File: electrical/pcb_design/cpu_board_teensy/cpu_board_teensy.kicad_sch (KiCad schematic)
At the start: 9 parts, among them J1 Molex_504050-1291, U1 Teensy4.0_TopPinsOnly, U2 RFM69HCW, U3 BNO085_Adafruit_Breakout_I2C, U4 BMP390_Adafruit_Breakout

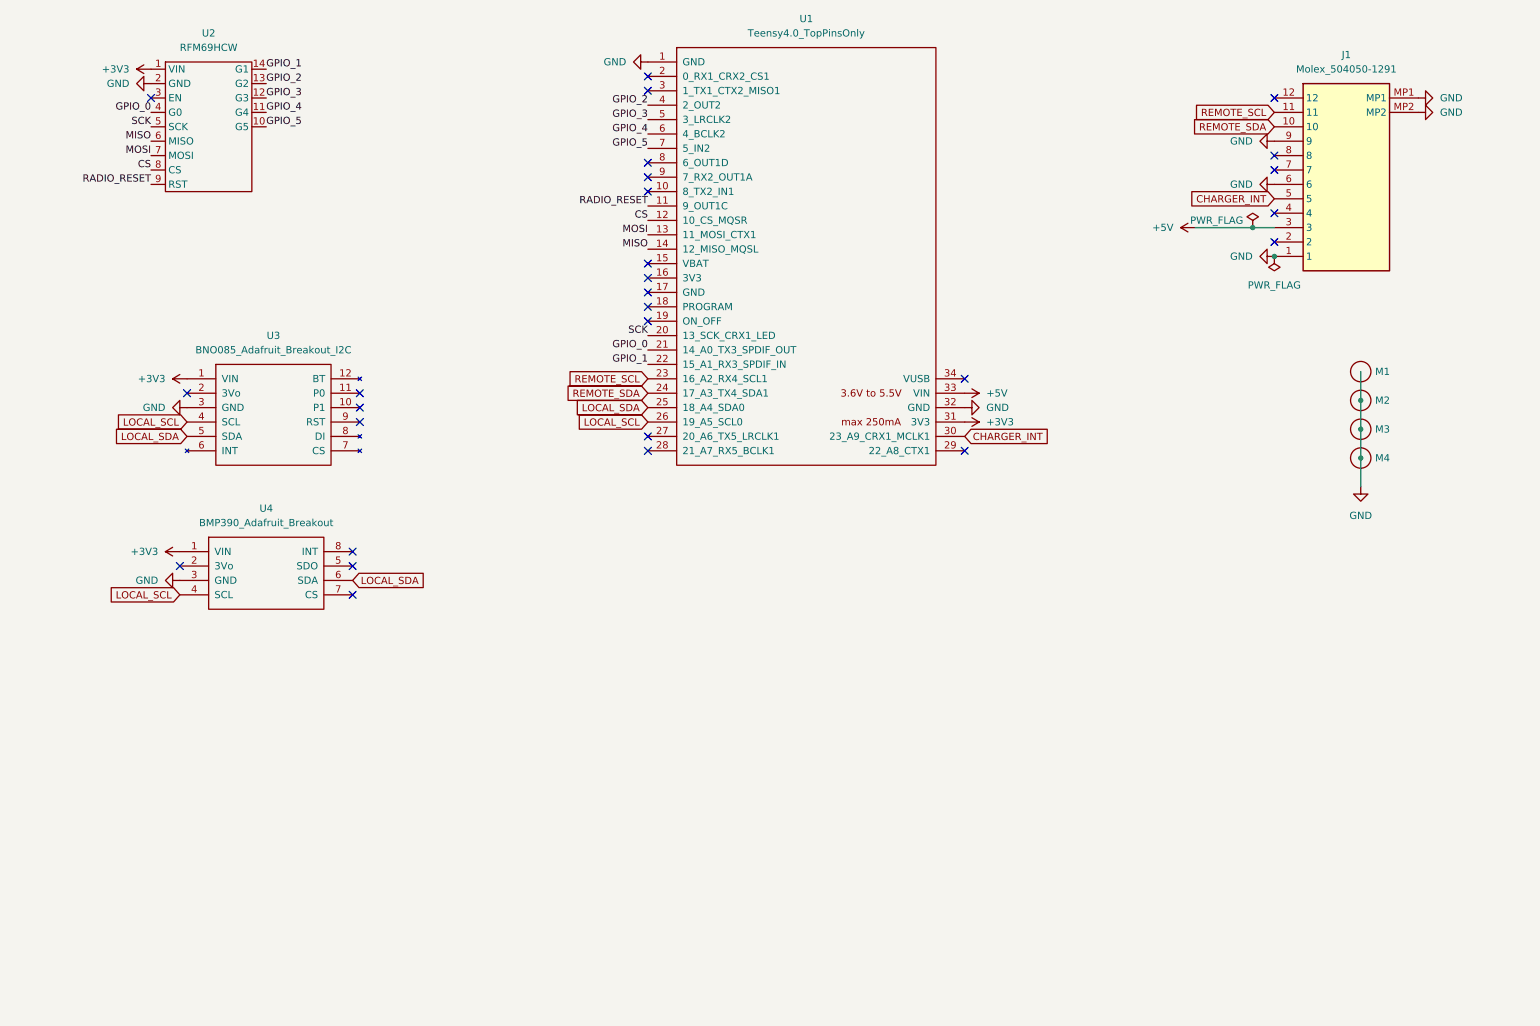
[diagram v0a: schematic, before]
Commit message: Adding support for PWM signals to magnetorquers and heating shroud.
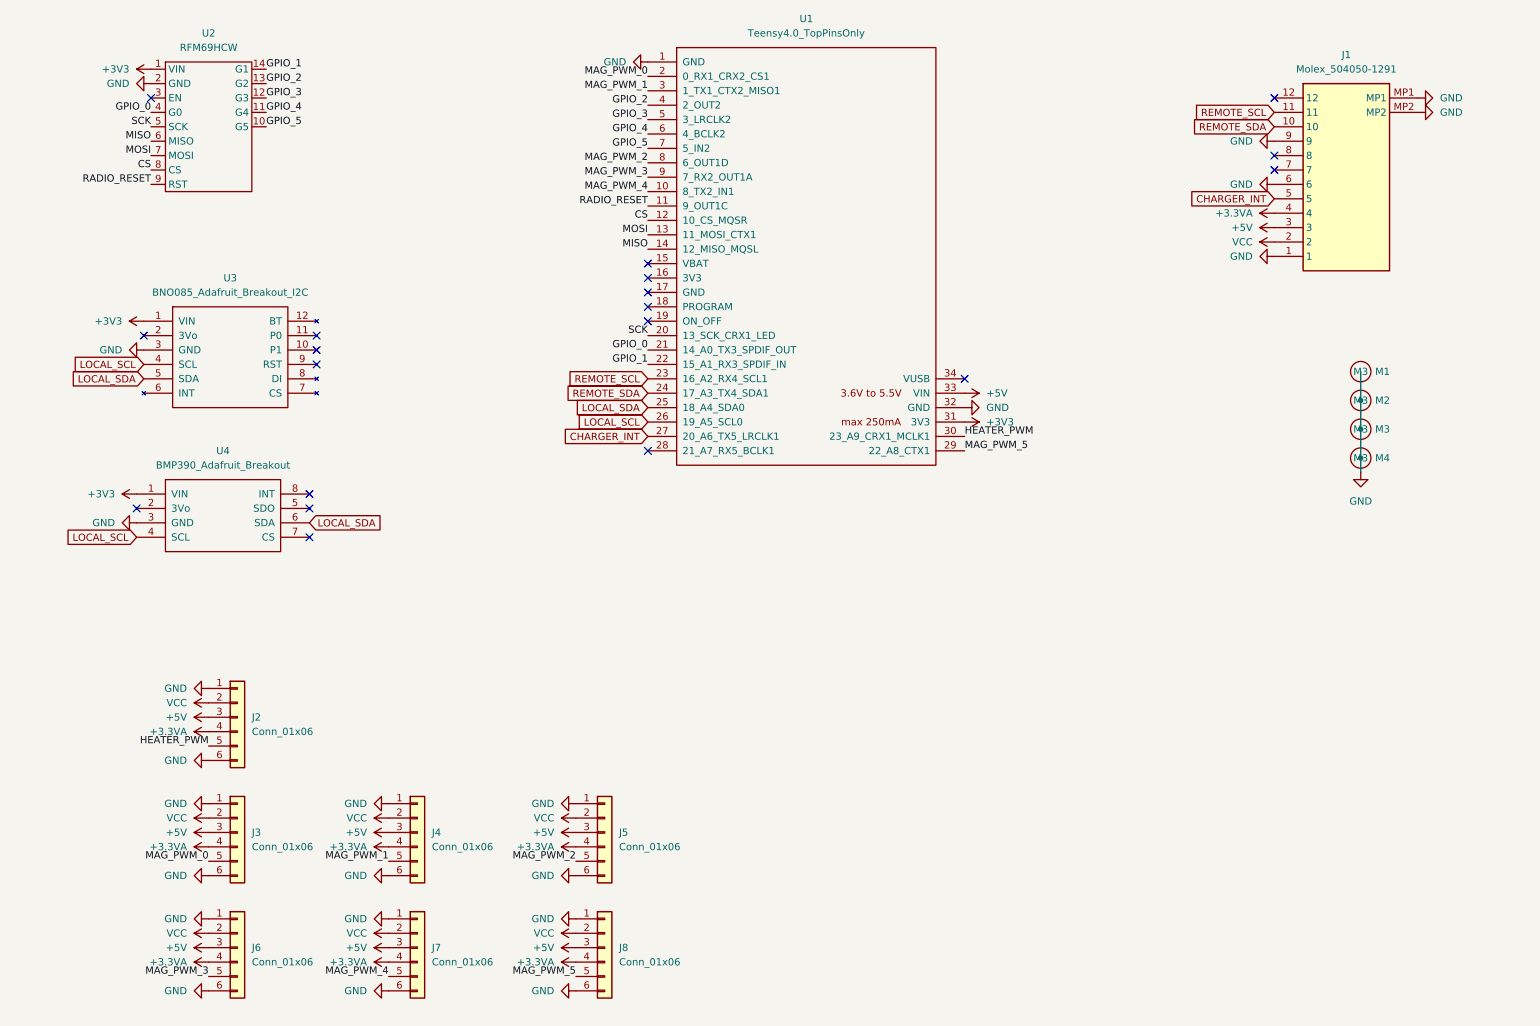
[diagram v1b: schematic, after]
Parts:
- added J2, J3, J4, J5, J6, J7, J8: Conn_01x06, symbol Connector_Generic:Conn_01x06
- M1, M2, M3, M4: value ~ -> M3
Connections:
- net +5V: now also J2.3 (Pin_3), J3.3 (Pin_3), J4.3 (Pin_3), J5.3 (Pin_3), J6.3 (Pin_3), J7.3 (Pin_3), J8.3 (Pin_3)
- net CHARGER_INT: now also U1.27 (20_A6_TX5_LRCLK1); no longer U1.30 (23_A9_CRX1_MCLK1)
- net GND: now also J2.1 (Pin_1), J2.6 (Pin_6), J3.1 (Pin_1), J3.6 (Pin_6), J4.1 (Pin_1), J4.6 (Pin_6), J5.1 (Pin_1), J5.6 (Pin_6), J6.1 (Pin_1), J6.6 (Pin_6), J7.1 (Pin_1), J7.6 (Pin_6), J8.1 (Pin_1), J8.6 (Pin_6)
- net MAG_PWM_4: now reaches U1.10 (8_TX2_IN1)
- net MAG_PWM_4: now also J7.5 (Pin_5)
- net MAG_PWM_0: now reaches U1.2 (0_RX1_CRX2_CS1)
- net MAG_PWM_0: now also J3.5 (Pin_5)
- net MAG_PWM_5: now reaches U1.29 (22_A8_CTX1)
- net MAG_PWM_5: now also J8.5 (Pin_5)
- net MAG_PWM_1: now reaches U1.3 (1_TX1_CTX2_MISO1)
- net MAG_PWM_1: now also J4.5 (Pin_5)
- net MAG_PWM_2: now reaches U1.8 (6_OUT1D)
- net MAG_PWM_2: now also J5.5 (Pin_5)
- net MAG_PWM_3: now reaches U1.9 (7_RX2_OUT1A)
- net MAG_PWM_3: now also J6.5 (Pin_5)
- net VCC: now reaches J1.2
- net VCC: now also J2.2 (Pin_2), J3.2 (Pin_2), J4.2 (Pin_2), J5.2 (Pin_2), J6.2 (Pin_2), J7.2 (Pin_2), J8.2 (Pin_2)
- net +3.3VA: now reaches J1.4
- net +3.3VA: now also J2.4 (Pin_4), J3.4 (Pin_4), J4.4 (Pin_4), J5.4 (Pin_4), J6.4 (Pin_4), J7.4 (Pin_4), J8.4 (Pin_4)
- new net HEATER_PWM: J2.5 (Pin_5), U1.30 (23_A9_CRX1_MCLK1)
- no-connect marks 28 -> 19
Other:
- moved on the sheet: U3, U4

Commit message: Finished iteration on Teensy CPU board
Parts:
- removed J2, J3, J4, J5, J6, J7, J8: Conn_01x06, symbol Connector_Generic:Conn_01x06
- added J2: HEATER_PWM, footprints:Molex_5013310607, symbol TVSC:CPU_PWM_Header
- added J3: MAGNETORQUER_PWM_0, footprints:Molex_5013310607, symbol TVSC:CPU_PWM_Header
- added J4: MAGNETORQUER_PWM_1, footprints:Molex_5013310607, symbol TVSC:CPU_PWM_Header
- added J5: MAGNETORQUER_PWM_2, footprints:Molex_5013310607, symbol TVSC:CPU_PWM_Header
- added J6: MAGNETORQUER_PWM_3, footprints:Molex_5013310607, symbol TVSC:CPU_PWM_Header
- added J7: MAGNETORQUER_PWM_4, footprints:Molex_5013310607, symbol TVSC:CPU_PWM_Header
- added J8: MAGNETORQUER_PWM_5, footprints:Molex_5013310607, symbol TVSC:CPU_PWM_Header
- J1: footprint 5040501291 -> footprints:5040501291; Height 2.15 -> (none); Manufacturer (none) -> Molex; Manufacturer Part Number (none) -> 504050-1291; Manufacturer_Name Molex -> (none); Manufacturer_Part_Number 504050-1291 -> (none); Mouser Part Number 538-504050-1291 -> (none); Mouser Price/Stock https://www.mouser.co.uk/ProductDetail/Molex/504050-1291?qs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 -> (none)
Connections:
- net +3.3VA: now also J2.4 (+3.3V), J3.4 (+3.3V), J4.4 (+3.3V), J5.4 (+3.3V), J6.4 (+3.3V), J7.4 (+3.3V), J8.4 (+3.3V)
- net +5V: now also J2.3 (+5V), J3.3 (+5V), J4.3 (+5V), J5.3 (+5V), J6.3 (+5V), J7.3 (+5V), J8.3 (+5V)
- net GND: now also J2.1 (GND), J2.6 (GND2), J2.7 (MP1), J2.8 (MP2), J3.1 (GND), J3.6 (GND2), J3.7 (MP1), J3.8 (MP2), J4.1 (GND), J4.6 (GND2), J4.7 (MP1), J4.8 (MP2), J5.1 (GND), J5.6 (GND2), J5.7 (MP1), J5.8 (MP2), J6.1 (GND), J6.6 (GND2), J6.7 (MP1), J6.8 (MP2), J7.1 (GND), J7.6 (GND2), J7.7 (MP1), J7.8 (MP2), J8.1 (GND), J8.6 (GND2), J8.7 (MP1), J8.8 (MP2)
- net HEATER_PWM: now also J2.5 (PWM)
- net MAG_PWM_0: now also J3.5 (PWM)
- net MAG_PWM_1: now also J4.5 (PWM)
- net MAG_PWM_2: now also J5.5 (PWM)
- net MAG_PWM_3: now also J6.5 (PWM)
- net MAG_PWM_4: now also J7.5 (PWM)
- net MAG_PWM_5: now also J8.5 (PWM)
- net VCC: now also J2.2 (VCC), J3.2 (VCC), J4.2 (VCC), J5.2 (VCC), J6.2 (VCC), J7.2 (VCC), J8.2 (VCC)
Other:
- moved on the sheet: M1, M2, M3, M4, U3, U4

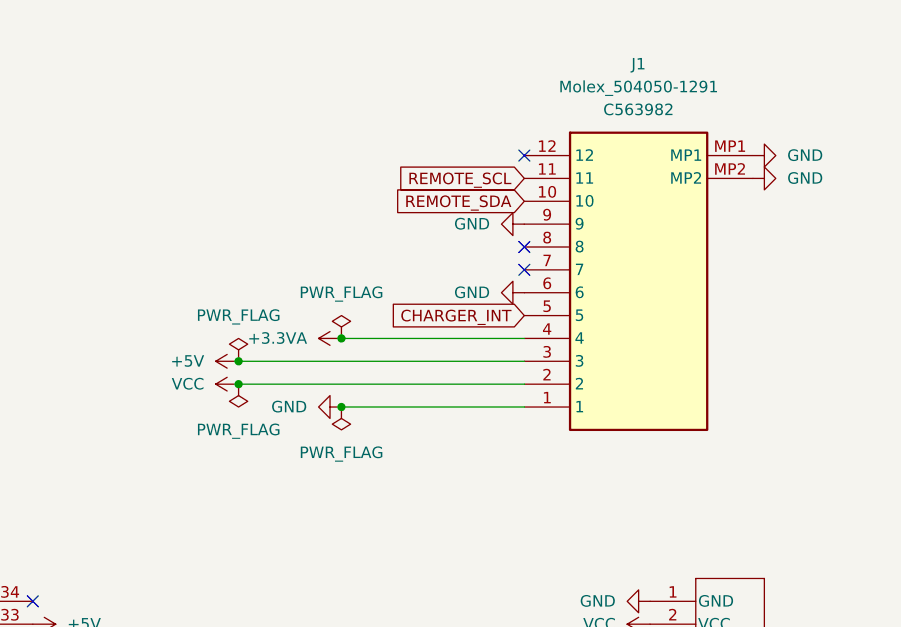
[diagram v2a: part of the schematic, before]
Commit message: Fixed major bug where header orientations need to be swapped on different ends of the cabling.
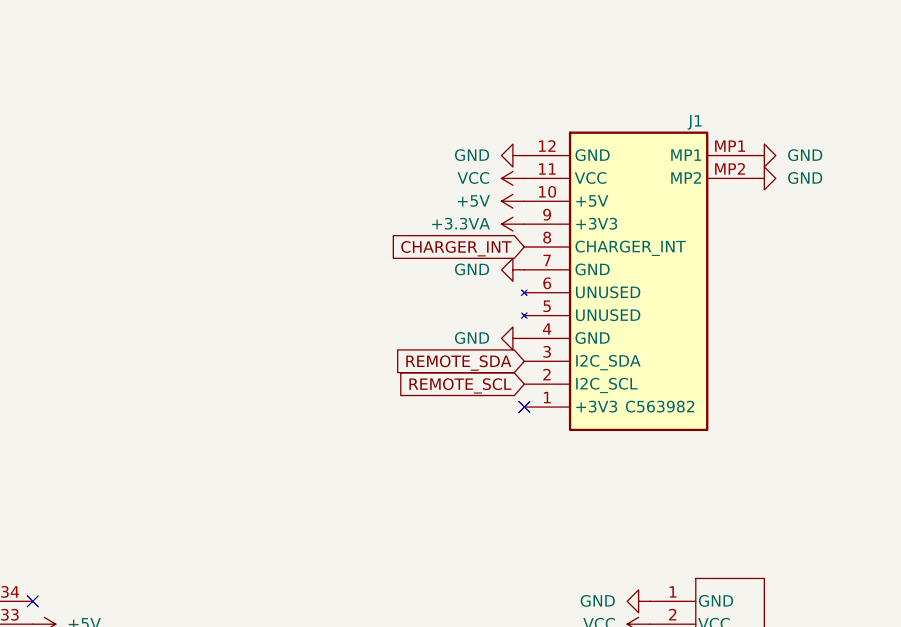
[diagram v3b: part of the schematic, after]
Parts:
- J1: value Molex_504050-1291 -> Interconnect_Power_CPU-Power_side; symbol TVSC:Molex_504050-1291 -> TVSC:Interconnect_Power_CPU-CPU_side
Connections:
- net +3.3VA: now also J1.9 (+3V3); no longer J1.4
- net +5V: now also J1.10 (+5V); no longer J1.3
- net CHARGER_INT: now also J1.8 (CHARGER_INT); no longer J1.5
- net GND: now also J1.12 (GND), J1.4 (GND), J1.7 (GND); no longer J1.1, J1.6, J1.9
- net REMOTE_SCL: now also J1.2 (I2C_SCL); no longer J1.11
- net REMOTE_SDA: now also J1.3 (I2C_SDA); no longer J1.10
- net VCC: now also J1.11 (VCC); no longer J1.2
- no-connect marks 19 -> 17
